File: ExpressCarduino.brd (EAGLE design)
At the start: 38.8 x 27.7 mm, 15 parts, among them IC2 MCP23008, U1 AP3012

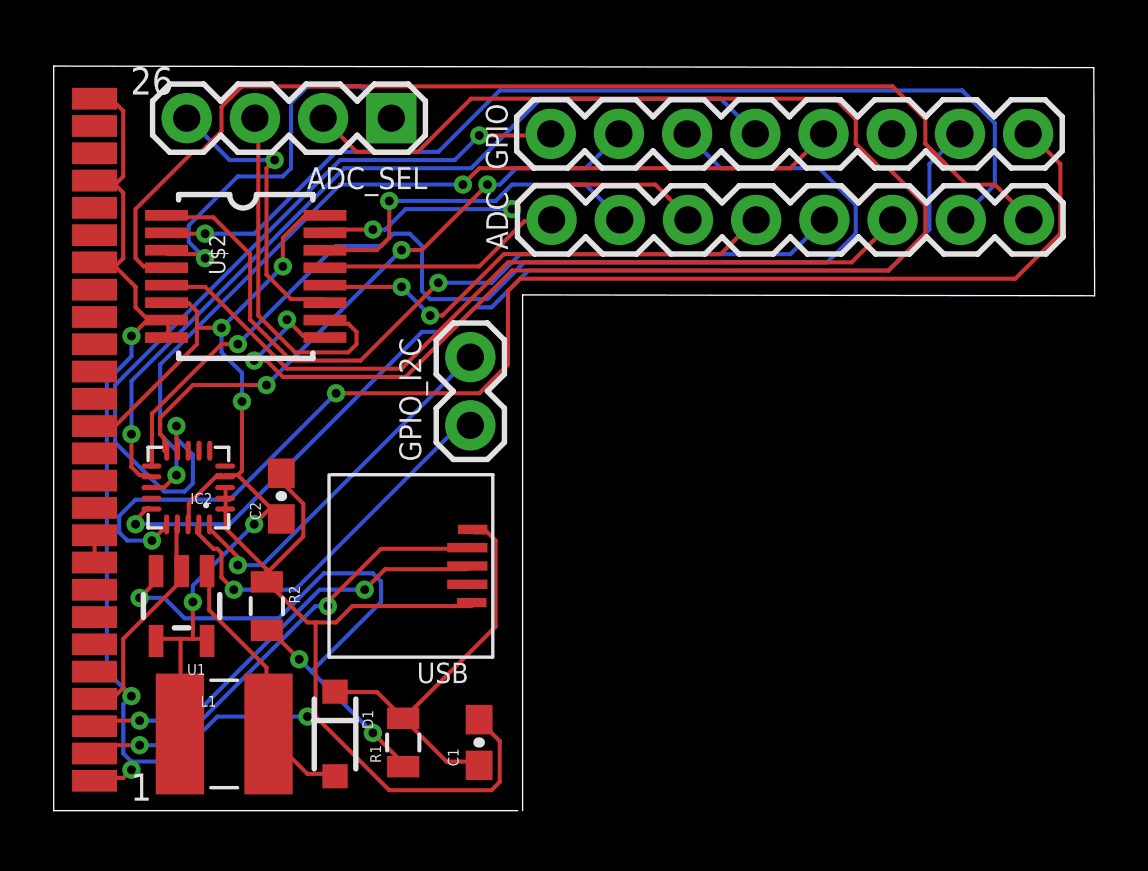
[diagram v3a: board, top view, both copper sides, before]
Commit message: Isolated the USB circuit from the other ICs
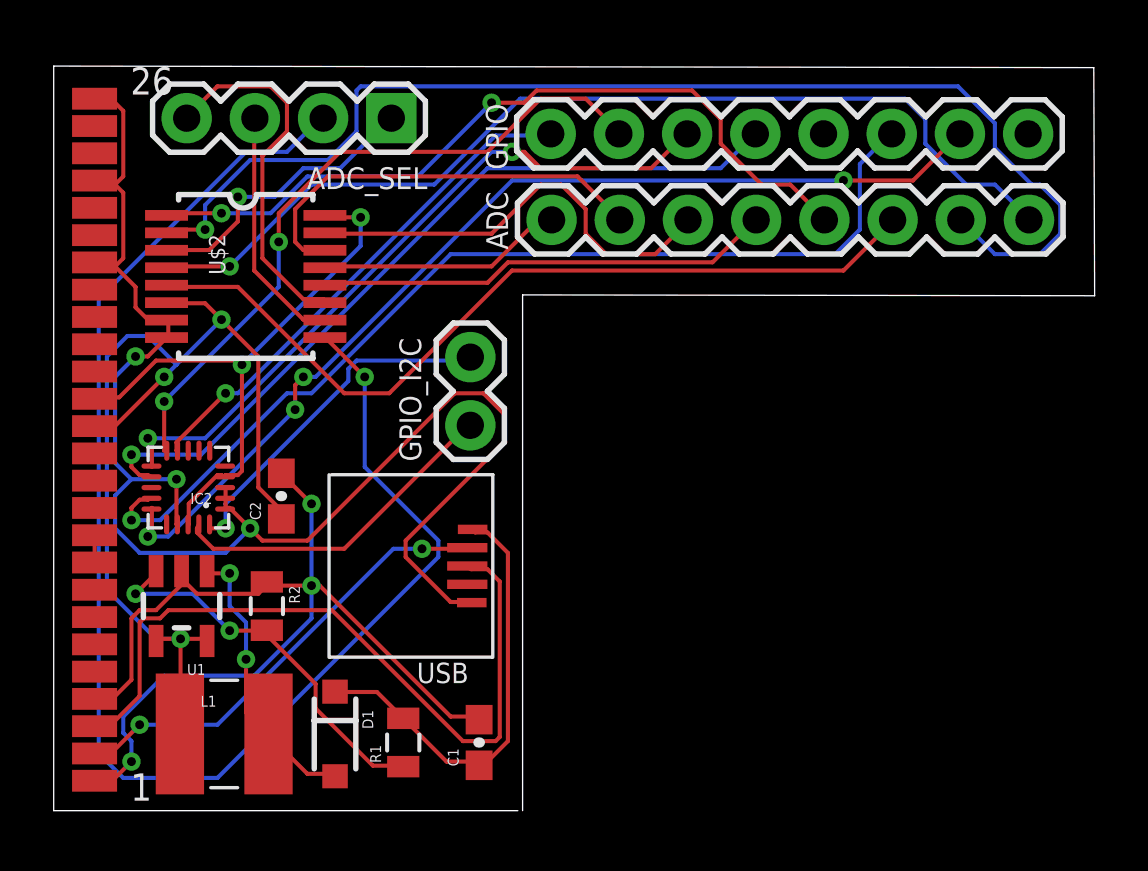
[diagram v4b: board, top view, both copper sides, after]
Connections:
- removed net 3.3V_A: C2.1, IC2.18, IC2.4, L1.P$1, U$1.P$14, U$2.16, U$2.6, U1.4, U1.5
- removed net 3.3V_AUX: U$1.P$12
- removed net 3.3V_B: U$1.P$15
- new net GND_USB: C1.2, C2.2, R2.1, U$1.P$1, U$1.P$4, U1.2
- new net VCC: IC2.18, IC2.4, U$1.P$15, U$2.16
- new net VUSB: C2.1, L1.P$1, U$1.P$14, U$2.6, U1.4, U1.5
- net GND: no longer C1.2, C2.2, R2.1, U$1.P$1, U$1.P$4, U1.2
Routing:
- net N$10: track 48.0 -> 0.00 mm, vias 2 -> 0
- net GND_USB: track 0.00 -> 38.9 mm, vias 0 -> 3
- net 3.3V_A: track 38.1 -> 0.00 mm, vias 5 -> 0
- net VUSB: track 0.00 -> 38.1 mm, vias 0 -> 3
- net N$8: track 0.00 -> 37.0 mm, vias 0 -> 1
- net N$7: track 33.8 -> 0.00 mm, vias 2 -> 0
- net GND: track 83.5 -> 57.0 mm, vias 4 -> 3
- net VCC: track 0.00 -> 22.1 mm, vias 0 -> 2
- net N$5: track 42.5 -> 26.4 mm, vias 1 -> 2
- net USBD+: track 16.4 -> 27.8 mm, vias 2 -> 0
- net N$2: track 29.4 -> 19.0 mm, vias 2 -> 1
- net N$1: track 23.2 -> 14.5 mm, vias 3 -> 2
- net N$25: track 37.7 -> 45.0 mm
- net N$30: track 13.6 -> 9.08 mm
- net N$26: track 41.4 -> 37.1 mm, vias 0 -> 1
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
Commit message: Updated with correct measurements for the USB plug and swaped out the 8bit expander for the 16
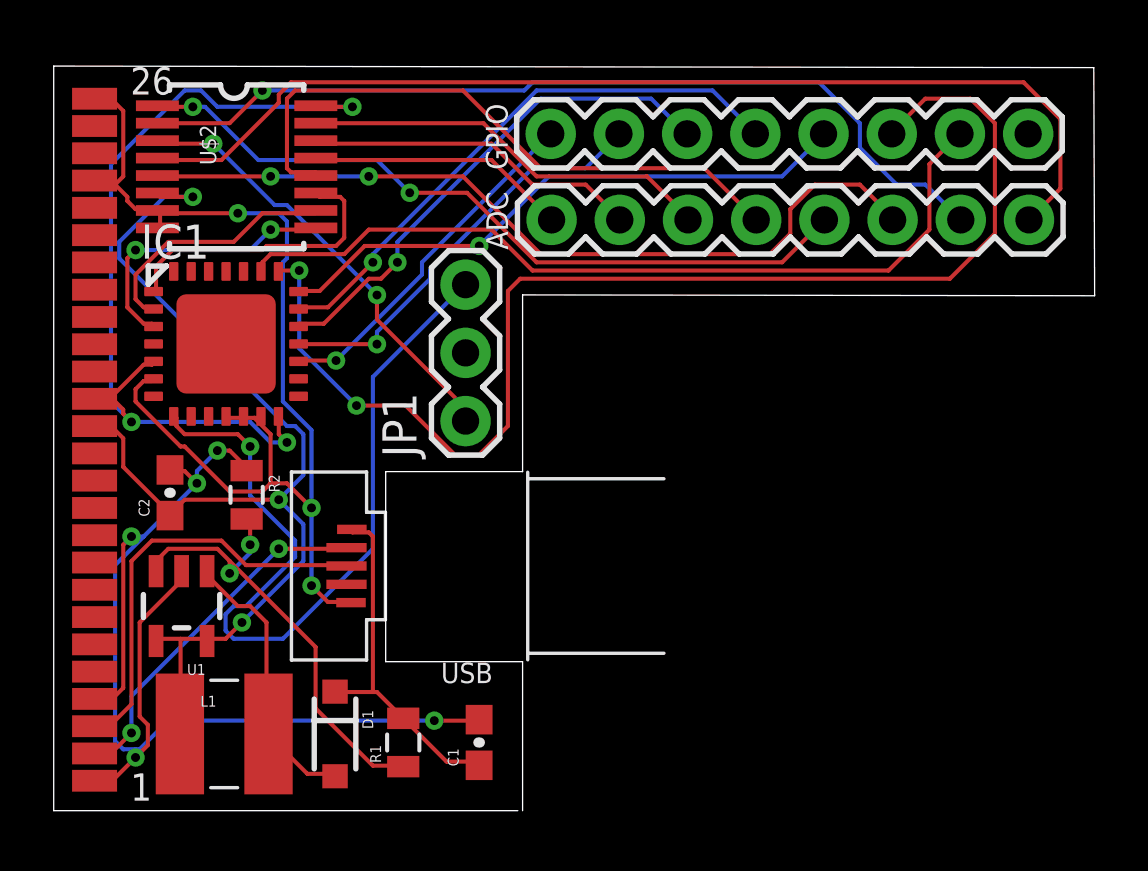
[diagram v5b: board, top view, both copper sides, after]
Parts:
- removed ADC_SEL: (no value), SparkFun-Connectors:1X04
- removed GPIO_I2C: (no value), SparkFun-Connectors:1X02
- removed IC2: MCP23008, HokieGeek:QFN-20-0.4MM-V2
- added IC1: MCP23017ML, adafruit:QFN28-ML_6X6MM
- added JP1: (no value), SparkFun-Connectors:1X03
- moved R2 4.21 mm to (7.19, 11.8)
- moved C2 4.15 mm to (4.33, 11.8)
- moved U$2 4.10 mm to (6.71, 24.0)
- moved USB 1.01 mm to (12.6, 9.11)
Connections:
- removed net 1.5V: U$1.P$10, U$1.P$9
- removed net N$11: GPIO_I2C.1, IC2.19
- removed net N$12: GPIO_I2C.2, IC2.20
- removed net N$13: ADC_SEL.1, U$2.3
- removed net N$29: ADC_SEL.2, U$2.9
- removed net N$30: ADC_SEL.3, U$2.10
- removed net N$31: ADC_SEL.4, U$2.11
- new net GPIO_SCL: IC1.8, JP1.3
- new net GPIO_SDA: IC1.9, JP1.2
- new net MUX_A: IC1.1, U$2.11
- new net MUX_B: IC1.2, U$2.10
- new net MUX_C: IC1.3, U$2.9
- new net MUX_COM: JP1.1, U$2.3
- net GND: now also IC1.11, IC1.12, IC1.13, IC1.6; no longer IC2.1, IC2.17, IC2.2, IC2.3
- net N$10: now also IC1.24; no longer IC2.16
- net N$2: now also IC1.17; no longer IC2.9
- net N$4: now also IC1.18; no longer IC2.10
- net N$5: now also IC1.19; no longer IC2.11
- net N$6: now also IC1.20; no longer IC2.12
- net N$7: now also IC1.21; no longer IC2.13
- net N$8: now also IC1.22; no longer IC2.14
- net N$9: now also IC1.23; no longer IC2.15
- net VCC: now also IC1.14, IC1.5; no longer IC2.18, IC2.4
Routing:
- net N$29: track 54.4 -> 0.00 mm, vias 1 -> 0
- net GPIO_SCL: track 0.00 -> 30.6 mm, vias 0 -> 1
- net N$7: track 0.00 -> 22.0 mm, vias 0 -> 1
- net MUX_COM: track 0.00 -> 16.6 mm, vias 0 -> 2
- net GND: track 57.0 -> 43.1 mm
- net N$31: track 13.7 -> 0.00 mm
- net N$12: track 13.3 -> 0.00 mm, vias 1 -> 0
- net N$11: track 12.6 -> 0.00 mm
- net USBD+: track 27.8 -> 15.8 mm
- net N$25: track 45.0 -> 33.2 mm
- net VCC: track 22.1 -> 33.6 mm, vias 2 -> 3
- net MUX_A: track 0.00 -> 11.0 mm
- net N$13: track 10.9 -> 0.00 mm, vias 1 -> 0
- net MUX_C: track 0.00 -> 10.6 mm, vias 0 -> 2
- net N$4: track 25.7 -> 15.6 mm, vias 2 -> 1
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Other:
- outline, holes or cut-outs redrawn

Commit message: Fixed pins for the mux and rearranged the board for better routing
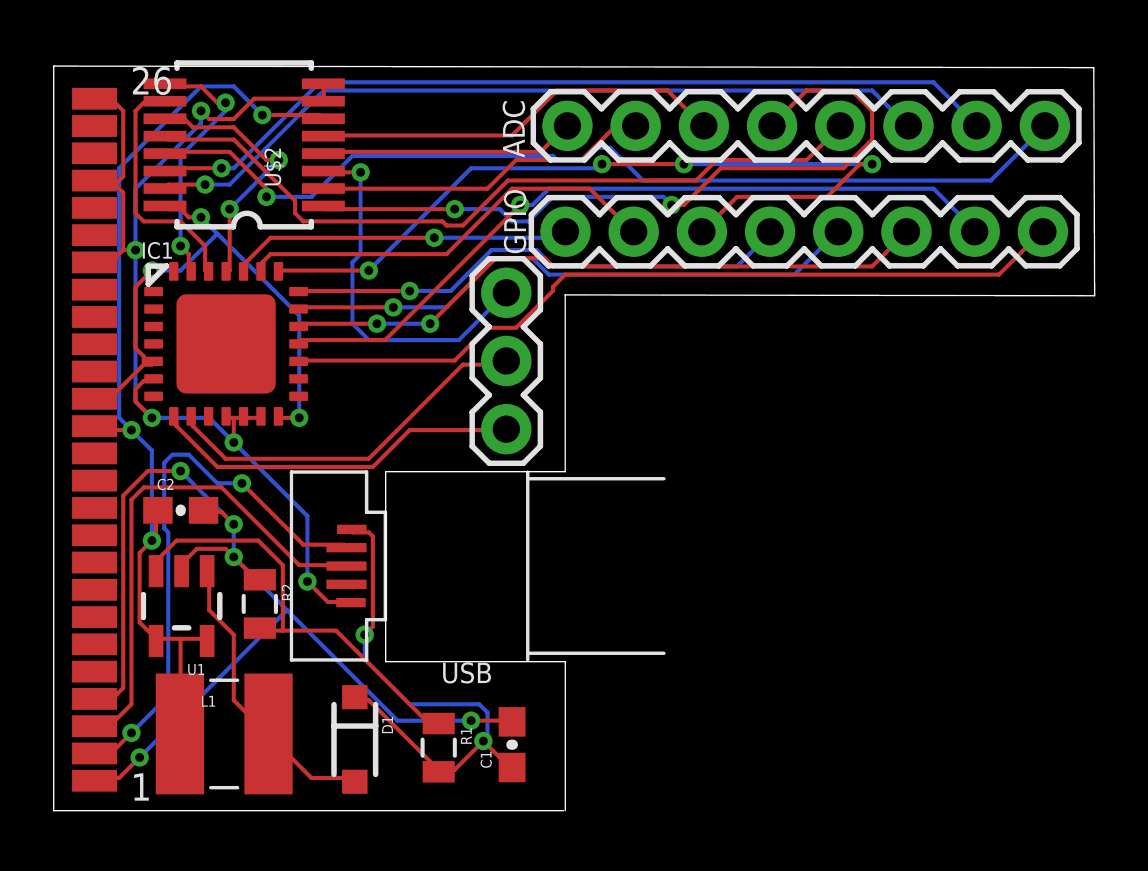
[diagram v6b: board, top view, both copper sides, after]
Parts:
- moved ADC 18.7 mm to (36.9, 25.5), turned to 180 degrees
- moved GPIO 18.7 mm to (36.8, 21.6), turned to 180 degrees
- moved JP1 5.01 mm to (16.9, 19.3), turned to 270 degrees
- moved R2 4.09 mm to (7.68, 7.70)
- moved R1 1.33 mm to (14.3, 2.35), turned to 270 degrees
- moved C1 1.23 mm to (17.1, 2.46)
- moved U$2 0.86 mm to (7.19, 24.7), turned to 90 degrees
- moved C2 0.77 mm to (4.73, 11.2), turned to 0 degrees
- moved D1 0.76 mm to (11.2, 2.65)
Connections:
- net MUX_A: now also IC1.25; no longer IC1.1
- net MUX_B: now also IC1.26; no longer IC1.2
- net MUX_C: now also IC1.27; no longer IC1.3
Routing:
- net N$26: track 39.8 -> 9.54 mm
- net N$19: track 9.72 -> 35.9 mm, vias 0 -> 1
- net N$25: track 33.2 -> 12.6 mm, vias 1 -> 0
- net N$20: track 12.6 -> 32.3 mm, vias 0 -> 1
- net GPIO_SCL: track 30.6 -> 13.9 mm, vias 1 -> 0
- net N$2: track 13.2 -> 29.8 mm, vias 1 -> 0
- net N$24: track 30.8 -> 15.4 mm, vias 2 -> 0
- net N$8: track 46.5 -> 31.2 mm, vias 2 -> 4
- net N$9: track 31.0 -> 16.0 mm
- net N$21: track 15.4 -> 29.7 mm, vias 0 -> 1
- net GPIO_SDA: track 0.00 -> 14.1 mm
- net N$10: track 0.00 -> 12.8 mm, vias 0 -> 1
- net N$4: track 15.6 -> 28.3 mm
- net VCC: track 33.6 -> 21.0 mm
- net USBD-: track 13.4 -> 20.7 mm
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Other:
- outline, holes or cut-outs redrawn
